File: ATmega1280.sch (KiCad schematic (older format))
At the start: 23 parts, among them CON1 AVR-ISP-10, CON2 AVR-JTAG-10, IC1 ATMEGA1280-A, P1 CONN_02X20, SW1 SW_PUSH, U1 74HCT541_PWR, U5 CONN3, U6 WS2812, U7 WS2812, U8 WS2812, U9 CONN3, X1 CRYSTAL

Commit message: Изменения футпринтов и расположения на плате
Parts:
- removed U5: CONN3, Connect:Wafer_Horizontal10x5.8x7RM2.5-3, symbol CONN3
- removed U9: CONN3, Pin_Headers:Pin_Header_Angled_1x03, symbol CONN3
- added P3, P4: CONN_01X03, Pin_Headers:Pin_Header_Angled_1x03, symbol CONN_01X03
- C10, C11, C12, C9: footprint Capacitors_SMD:C_0402 -> Capacitors_SMD:C_0805
- R6: footprint Resistors_SMD:R_0402 -> Resistors_SMD:R_0805
- U1: footprint Display:HDSP-48xx -> Housings_SSOP:SSOP-20_5.3x7.2mm_Pitch0.65mm
- U6, U7, U8: footprint Connectors_Molex:Connector_Microfit3_Header_02x03_Straight_43045-0628 -> 5050:5050
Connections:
- net labels added: 35, 36, 37, 38, 39, 40, CE1
- net labels removed: 21, 23, 25, 27
- wire segments 189 -> 192
- no-connect marks 56 -> 53

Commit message: Питание и LM2596
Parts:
- C13, C21, C22, C7, C8: footprint Capacitors_SMD:C_0603_HandSoldering -> Capacitors_SMD:C_0805
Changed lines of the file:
@@
 $EndComp
 $Comp
-L +5V #PWR03
+L +5V #PWR02
 U 1 1 56E703CC
 P 3500 900
-F 0 "#PWR03" H 3500 750 50  0001 C CNN
+F 0 "#PWR02" H 3500 750 50  0001 C CNN
 F 1 "+5V" H 3500 1040 50  0000 C CNN
 F 2 "" H 3500 900 50  0000 C CNN
@@
 $EndComp
 $Comp
-L GND #PWR04
+L GND #PWR03
 U 1 1 56E704E1
 P 4450 7500
-F 0 "#PWR04" H 4450 7250 50  0001 C CNN
+F 0 "#PWR03" H 4450 7250 50  0001 C CNN
 F 1 "GND" H 4450 7350 50  0000 C CNN
 F 2 "" H 4450 7500 50  0000 C CNN
@@
 F 0 "C22" H 1975 3200 50  0000 L CNN
 F 1 "27pF" H 1975 3000 50  0000 L CNN
-F 2 "Capacitors_SMD:C_0603_HandSoldering" H 1988 2950 50  0001 C CNN
+F 2 "Capacitors_SMD:C_0805" H 1988 2950 50  0001 C CNN
 F 3 "" H 1950 3100 50  0000 C CNN
 	1    1950 3100
@@
 F 0 "C21" H 2675 3200 50  0000 L CNN
 F 1 "27pF" H 2675 3000 50  0000 L CNN
-F 2 "Capacitors_SMD:C_0603_HandSoldering" H 2688 2950 50  0001 C CNN
+F 2 "Capacitors_SMD:C_0805" H 2688 2950 50  0001 C CNN
 F 3 "" H 2650 3100 50  0000 C CNN
 	1    2650 3100
@@
 $EndComp
 $Comp
-L GND #PWR05
+L GND #PWR04
 U 1 1 56E707E0
 P 2650 3550
-F 0 "#PWR05" H 2650 3300 50  0001 C CNN
+F 0 "#PWR04" H 2650 3300 50  0001 C CNN
 F 1 "GND" H 2650 3400 50  0000 C CNN
 F 2 "" H 2650 3550 50  0000 C CNN
@@
 $EndComp
 $Comp
-L GND #PWR06
+L GND #PWR05
 U 1 1 56E70DCE
 P 10150 3600
-F 0 "#PWR06" H 10150 3350 50  0001 C CNN
+F 0 "#PWR05" H 10150 3350 50  0001 C CNN
 F 1 "GND" H 10150 3450 50  0000 C CNN
 F 2 "" H 10150 3600 50  0000 C CNN
@@
 MISO
 $Comp
-L GND #PWR07
+L GND #PWR06
 U 1 1 56E711C0
 P 10350 1700
-F 0 "#PWR07" H 10350 1450 50  0001 C CNN
+F 0 "#PWR06" H 10350 1450 50  0001 C CNN
 F 1 "GND" H 10350 1550 50  0000 C CNN
 F 2 "" H 10350 1700 50  0000 C CNN
@@
 RESET
 $Comp
-L +5V #PWR08
+L +5V #PWR07
 U 1 1 56E711D2
 P 10350 800
-F 0 "#PWR08" H 10350 650 50  0001 C CNN
+F 0 "#PWR07" H 10350 650 50  0001 C CNN
 F 1 "+5V" H 10350 940 50  0000 C CNN
 F 2 "" H 10350 800 50  0000 C CNN
@@
 Vcc
 $Comp
-L +5V #PWR09
+L +5V #PWR08
 U 1 1 56F4EFCF
 P 10150 2500
-F 0 "#PWR09" H 10150 2350 50  0001 C CNN
+F 0 "#PWR08" H 10150 2350 50  0001 C CNN
 F 1 "+5V" H 10150 2640 50  0000 C CNN
 F 2 "" H 10150 2500 50  0000 C CNN
@@
 $EndComp
 $Comp
-L GND #PWR010
+L GND #PWR09
 U 1 1 56F4F102
 P 1450 2000
-F 0 "#PWR010" H 1450 1750 50  0001 C CNN
+F 0 "#PWR09" H 1450 1750 50  0001 C CNN
 F 1 "GND" H 1450 1850 50  0000 C CNN
 F 2 "" H 1450 2000 50  0000 C CNN
@@
 A7
 $Comp
-L GND #PWR011
+L GND #PWR010
 U 1 1 5706A0E3
 P 7550 3150
-F 0 "#PWR011" H 7550 2900 50  0001 C CNN
+F 0 "#PWR010" H 7550 2900 50  0001 C CNN
 F 1 "GND" H 7550 3000 50  0000 C CNN
 F 2 "" H 7550 3150 50  0000 C CNN
@@
 NoConn ~ 3150 4550
 $Comp
-L GND #PWR012
+L GND #PWR011
 U 1 1 5717E47B
 P 9400 5900
-F 0 "#PWR012" H 9400 5650 50  0001 C CNN
+F 0 "#PWR011" H 9400 5650 50  0001 C CNN
 F 1 "GND" H 9400 5750 50  0000 C CNN
 F 2 "" H 9400 5900 50  0000 C CNN
@@
 TXD0
 $Comp
-L GND #PWR013
+L GND #PWR012
 U 1 1 571E463B
 P 10400 5350
-F 0 "#PWR013" H 10400 5100 50  0001 C CNN
+F 0 "#PWR012" H 10400 5100 50  0001 C CNN
 F 1 "GND" H 10400 5200 50  0000 C CNN
 F 2 "" H 10400 5350 50  0000 C CNN
@@
 $EndComp
 $Comp
-L +5V #PWR014
+L +5V #PWR013
 U 1 1 571E941D
 P 1050 3900
-F 0 "#PWR014" H 1050 3750 50  0001 C CNN
+F 0 "#PWR013" H 1050 3750 50  0001 C CNN
 F 1 "+5V" H 1050 4040 50  0000 C CNN
 F 2 "" H 1050 3900 50  0000 C CNN
@@
 F 0 "C7" H 1675 4250 50  0000 L CNN
 F 1 "10nF" H 1675 4050 50  0000 L CNN
-F 2 "Capacitors_SMD:C_0603_HandSoldering" H 1688 4000 50  0001 C CNN
+F 2 "Capacitors_SMD:C_0805" H 1688 4000 50  0001 C CNN
 F 3 "" H 1650 4150 50  0000 C CNN
 	1    1650 4150
@@
 	1900 4450 3150 4450
 $Comp
-L GND #PWR015
+L GND #PWR014
 U 1 1 571E963E
 P 650 7150
-F 0 "#PWR015" H 650 6900 50  0001 C CNN
+F 0 "#PWR014" H 650 6900 50  0001 C CNN
 F 1 "GND" H 650 7000 50  0000 C CNN
 F 2 "" H 650 7150 50  0000 C CNN
@@
 F 0 "C8" H 1725 5250 50  0000 L CNN
 F 1 "10nF" H 1725 5050 50  0000 L CNN
-F 2 "Capacitors_SMD:C_0603_HandSoldering" H 1738 5000 50  0001 C CNN
+F 2 "Capacitors_SMD:C_0805" H 1738 5000 50  0001 C CNN
 F 3 "" H 1700 5150 50  0000 C CNN
 	1    1700 5150
@@
 F 0 "C13" H 1775 6450 50  0000 L CNN
 F 1 "10nF" H 1775 6250 50  0000 L CNN
-F 2 "Capacitors_SMD:C_0603_HandSoldering" H 1788 6200 50  0001 C CNN
+F 2 "Capacitors_SMD:C_0805" H 1788 6200 50  0001 C CNN
 F 3 "" H 1750 6350 50  0000 C CNN
 	1    1750 6350
@@
 	1800 5600 2100 5600
 $Comp
+L +5V #PWR015
+U 1 1 571EC74C
+P 950 4900
+F 0 "#PWR015" H 950 4750 50  0001 C CNN
+F 1 "+5V" H 950 5040 50  0000 C CNN
+F 2 "" H 950 4900 50  0000 C CNN
+F 3 "" H 950 4900 50  0000 C CNN
+	1    950  4900
+	1    0    0    -1
+$EndComp
+$Comp
 L +5V #PWR016
-U 1 1 571EC74C
+U 1 1 571EC7A2
 P 950 4900
 F 0 "#PWR016" H 950 4750 50  0001 C CNN
@@
 $Comp
 L +5V #PWR017
-U 1 1 571EC7A2
-P 950 4900
-F 0 "#PWR017" H 950 4750 50  0001 C CNN
-F 1 "+5V" H 950 5040 50  0000 C CNN
-F 2 "" H 950 4900 50  0000 C CNN
-F 3 "" H 950 4900 50  0000 C CNN
-	1    950  4900
-	1    0    0    -1
-$EndComp
-$Comp
-L +5V #PWR018
 U 1 1 571EC7E1
 P 1000 6000
-F 0 "#PWR018" H 1000 5850 50  0001 C CNN
+F 0 "#PWR017" H 1000 5850 50  0001 C CNN
 F 1 "+5V" H 1000 6140 50  0000 C CNN
 F 2 "" H 1000 6000 50  0000 C CNN
@@
 NoConn ~ 1050 6600
 $Comp
-L GND #PWR019
+L GND #PWR018
 U 1 1 571EDCF8
 P 2100 7150
-F 0 "#PWR019" H 2100 6900 50  0001 C CNN
+F 0 "#PWR018" H 2100 6900 50  0001 C CNN
 F 1 "GND" H 2100 7000 50  0000 C CNN
 F 2 "" H 2100 7150 50  0000 C CNN
@@
 $EndComp
 $Comp
-L +5V #PWR020
+L +5V #PWR019
 U 1 1 571EE571
 P 7550 1300
-F 0 "#PWR020" H 7550 1150 50  0001 C CNN
+F 0 "#PWR019" H 7550 1150 50  0001 C CNN
 F 1 "+5V" H 7550 1440 50  0000 C CNN
 F 2 "" H 7550 1300 50  0000 C CNN
@@
 Connection ~ 7300 6100
 $Comp
-L GND #PWR021
+L GND #PWR020
 U 1 1 57212B56
 P 7300 6300
-F 0 "#PWR021" H 7300 6050 50  0001 C CNN
+F 0 "#PWR020" H 7300 6050 50  0001 C CNN
 F 1 "GND" H 7300 6150 50  0000 C CNN
 F 2 "" H 7300 6300 50  0000 C CNN
@@
 	7150 5800 7150 5400
 $Comp
-L +5V #PWR022
+L +5V #PWR021
 U 1 1 57212CB0
 P 7150 5400
-F 0 "#PWR022" H 7150 5250 50  0001 C CNN
+F 0 "#PWR021" H 7150 5250 50  0001 C CNN
 F 1 "+5V" H 7150 5540 50  0000 C CNN
 F 2 "" H 7150 5400 50  0000 C CNN

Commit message: Готовая плата версия_1
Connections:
- net 17: no longer names the net of IC1.35 (PL0(ICP4))
- net RXD renamed RXD0
- net TXD renamed TXD0
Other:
- note added: "10"
- note added: "31"
- note added: "80"
- moved on the sheet: R6
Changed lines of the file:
@@
 LIBS:Pulse_Module-rescue
 LIBS:conn3
-LIBS:pl2303
 LIBS:power
 LIBS:device
@@
 L R R6
 U 1 1 56E703F2
-P 3150 1350
-F 0 "R6" V 3230 1350 50  0000 C CNN
-F 1 "R1" V 3150 1350 50  0000 C CNN
-F 2 "Resistors_SMD:R_0805" V 3080 1350 50  0001 C CNN
-F 3 "" H 3150 1350 50  0000 C CNN
-	1    3150 1350
+P 3020 1485
+F 0 "R6" V 3100 1485 50  0000 C CNN
+F 1 "R1" V 3020 1485 50  0000 C CNN
+F 2 "Resistors_SMD:R_0805" V 2950 1485 50  0001 C CNN
+F 3 "" H 3020 1485 50  0000 C CNN
+	1    3020 1485
 	1    0    0    -1
 $EndComp
@@
 L GND #PWR03
 U 1 1 56E704E1
-P 4450 7500
-F 0 "#PWR03" H 4450 7250 50  0001 C CNN
-F 1 "GND" H 4450 7350 50  0000 C CNN
-F 2 "" H 4450 7500 50  0000 C CNN
-F 3 "" H 4450 7500 50  0000 C CNN
-	1    4450 7500
+P 4450 7545
+F 0 "#PWR03" H 4450 7295 50  0001 C CNN
+F 1 "GND" H 4450 7395 50  0000 C CNN
+F 2 "" H 4450 7545 50  0000 C CNN
+F 3 "" H 4450 7545 50  0000 C CNN
+	1    4450 7545
 	1    0    0    -1
 $EndComp
@@
 Text Label 2900 1750 2    60   ~ 0
 RESET
-NoConn ~ 9400 1200
 $Comp
 L JUMPER JP1
@@
 	1    0    0    -1
 $EndComp
-Text HLabel 2550 1100 0    60   Input ~ 0
+Text HLabel 2475 1100 0    60   Input ~ 0
 Vcc
 $Comp
@@
 F0 "Sheet570520A0" 50
 F1 "pl2303.sch" 50
+F2 "TXD" I L 8100 4800 60
+F3 "RXD" I L 8100 4650 60
+F4 "RESET" I R 9050 4745 60
 $EndSheet
 $Comp
@@
 	1    0    0    -1
 $EndComp
-Text HLabel 8100 4650 2    60   Input ~ 0
-RXD
-Text HLabel 8100 4800 2    60   Input ~ 0
-TXD
 $Comp
 L 74HCT541_PWR U1
@@
 ALE
 NoConn ~ 6850 2750
-NoConn ~ 8800 2950
 Text Label 8600 3750 0    60   ~ 0
 35
@@
 Text Label 2900 6350 0    60   ~ 0
 RD
-Text HLabel 9050 4950 0    60   Input ~ 0
-RESET
-Text Label 9450 4950 2    60   ~ 0
+Text Label 9450 4745 2    60   ~ 0
 RESET
 Text Label 7800 4650 0    60   ~ 0
@@
 Connection ~ 4200 1100
 Connection ~ 4300 1100
-Wire Wire Line
-	3150 1750 3150 1500
-Wire Wire Line
-	3150 1200 3150 1100
 Connection ~ 3500 1100
 Wire Wire Line
@@
 	9800 1100 9200 1100
 Wire Wire Line
-	9800 1200 9400 1200
-Wire Wire Line
 	9200 1300 9800 1300
 Wire Wire Line
@@
 	4600 1100 4600 1450
 Wire Wire Line
-	9050 4950 9450 4950
+	9050 4745 9450 4745
 Wire Wire Line
 	8100 4650 7800 4650
@@
 Text Label 9500 3250 2    60   ~ 0
 A12
-Text Label 3000 2650 0    60   ~ 0
-17
 Text Label 3000 2750 0    60   ~ 0
 35
@@
 P 1650 4150
 F 0 "C7" H 1675 4250 50  0000 L CNN
-F 1 "10nF" H 1675 4050 50  0000 L CNN
+F 1 "10nF" V 1585 3910 50  0000 L CNN
 F 2 "Capacitors_SMD:C_0805" H 1688 4000 50  0001 C CNN
 F 3 "" H 1650 4150 50  0000 C CNN
@@
 	6450 5900 6050 5900
 Wire Wire Line
-	6450 6000 6050 6000
-Wire Wire Line
 	6450 6100 6050 6100
-NoConn ~ 6050 6000
 Text Label 6050 5700 0    60   ~ 0
 TCK
@@
 Text Label 6050 6950 2    60   ~ 0
 TDI
-Wire Wire Line
-	6700 5900 7100 5900
-Wire Wire Line
-	6700 6000 7100 6000
-NoConn ~ 7100 5900
-NoConn ~ 7100 6000
+NoConn ~ 6450 6000
 Wire Wire Line
 	6700 5700 7300 5700
@@
 40
 Wire Wire Line
-	3000 2650 3150 2650
-Wire Wire Line
 	3150 2750 3000 2750
 Wire Wire Line
@@
 NoConn ~ 3150 4150
 NoConn ~ 3150 4250
-NoConn ~ 3800 3450
 Wire Wire Line
 	5750 6250 6000 6250
@@
 Text Label 6000 6350 2    60   ~ 0
 CE2
+NoConn ~ 6700 6000
+NoConn ~ 6700 5900
+Wire Wire Line
+	2550 1100 2475 1100
+NoConn ~ 9800 1200
+NoConn ~ 8800 2950
+NoConn ~ 3150 2650
+Wire Wire Line
+	4450 7545 4450 7500
+Wire Wire Line
+	3020 1750 3020 1635
+Connection ~ 3020 1750
+Wire Wire Line
+	3020 1335 3020 1270
+Wire Wire Line
+	3020 1270 3205 1270
+Wire Wire Line
+	3205 1270 3205 1100
+Connection ~ 3205 1100
+Text Notes 9685 3235 0    60   ~ 0
+10
+Text Notes 10040 3245 0    60   ~ 0
+31
+Text Notes 10390 3240 0    60   ~ 0
+80
 $EndSCHEMATC

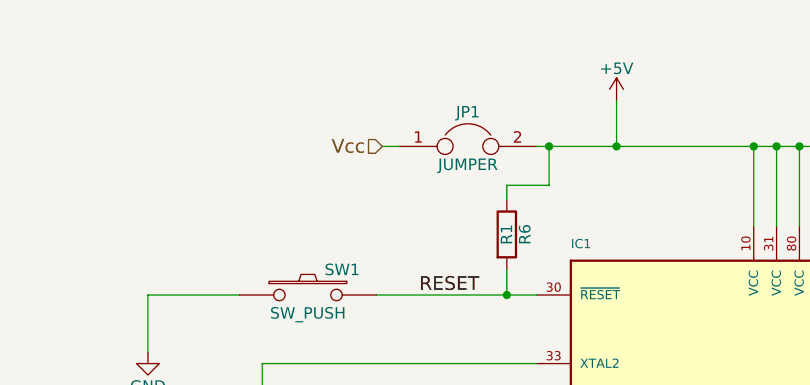
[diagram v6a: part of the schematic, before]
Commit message: разделение питания и добавление потенциометра у лмки
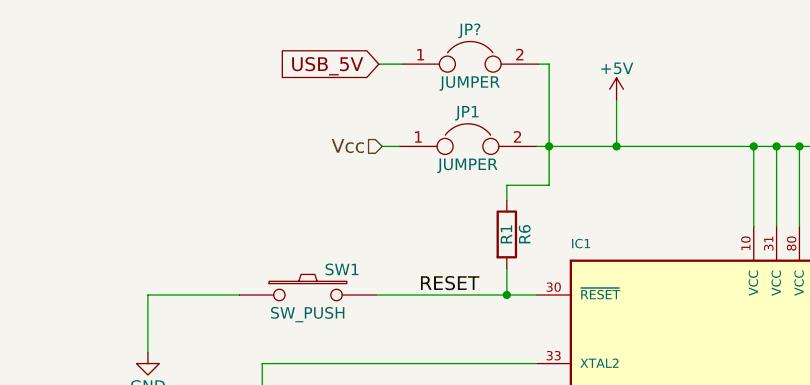
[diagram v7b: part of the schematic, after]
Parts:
- added JP?: JUMPER, symbol JUMPER
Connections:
- net +5V: now also JP?.2
- new net USB_5V: JP?.1
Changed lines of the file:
@@
 	3020 1335 3020 1270
 Wire Wire Line
-	3020 1270 3205 1270
+	3205 1270 3020 1270
 Wire Wire Line
-	3205 1270 3205 1100
+	3205 740  3205 1270
 Connection ~ 3205 1100
+Text GLabel 2460 740  0    60   Input ~ 0
+USB_5V
+$Comp
+L JUMPER JP?
+U 1 1 578E6590
+P 2860 740
+F 0 "JP?" H 2860 890 50  0000 C CNN
+F 1 "JUMPER" H 2860 660 50  0000 C CNN
+F 2 "" H 2860 740 50  0000 C CNN
+F 3 "" H 2860 740 50  0000 C CNN
+	1    2860 740
+	1    0    0    -1
+$EndComp
+Wire Wire Line
+	2460 740  2560 740
+Wire Wire Line
+	3160 740  3205 740
 $EndSCHEMATC
